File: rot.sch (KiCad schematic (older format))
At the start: 34 parts, among them J3 543630489, J4 M20-7830642, U2 W25Q32JVSSIQ_TR, U3 W25Q32JVSSIQ_TR, U4 W25Q32JVSSIQ_TR, U5 W25Q32JVSSIQ_TR

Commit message: RoT - cleanup
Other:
- note added: "RoT module connector"
- note removed: "RoT connector"
- moved on the sheet: J4
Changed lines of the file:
@@
 	1    0    0    -1
 $EndComp
-Text Notes 2425 1350 0    118  ~ 0
+Text Notes 1425 1250 0    118  ~ 24
 BIOS flash
-Text Notes 2525 6300 0    118  ~ 0
+Text Notes 1625 6175 0    118  ~ 24
 BMC flash
-Text Notes 10900 1500 0    118  ~ 0
+Text Notes 11525 4275 0    118  ~ 24
 TPM connector
 Text Notes 1650 6400 0    50   ~ 0
@@
 Wire Wire Line
 	9675 6025 9175 6025
-Text Notes 8325 4350 0    118  ~ 0
-RoT connector
+Text Notes 7375 4200 0    118  ~ 24
+RoT module connector
 Text Notes 8775 6950 0    50   ~ 0
 preliminary\n
@@
 L artix-dc-scm:M20-7830642 J4
 U 1 1 5FD63CCC
-P 11725 2200
-F 0 "J4" H 11725 2647 60  0000 C CNN
-F 1 "M20-7830642" H 11725 2541 60  0000 C CNN
-F 2 "artix-dc-scm-footprints:PinHeader_6x2_P2.54mm_Vertical" H 11925 2400 60  0001 L CNN
-F 3 "" H 11925 2500 60  0001 L CNN
-F 4 "M20-7830642" H 11925 2700 60  0001 L CNN "MPN"
-F 5 "Molex" H 11925 2800 60  0001 L CNN "Manufacturer"
-	1    11725 2200
-	1    0    0    -1
-$EndComp
-Text GLabel 10900 1950 1    50   Input ~ 0
+P 12475 5250
+F 0 "J4" H 12475 5697 60  0000 C CNN
+F 1 "M20-7830642" H 12475 5591 60  0000 C CNN
+F 2 "artix-dc-scm-footprints:PinHeader_6x2_P2.54mm_Vertical" H 12675 5450 60  0001 L CNN
+F 3 "" H 12675 5550 60  0001 L CNN
+F 4 "M20-7830642" H 12675 5750 60  0001 L CNN "MPN"
+F 5 "Molex" H 12675 5850 60  0001 L CNN "Manufacturer"
+	1    12475 5250
+	1    0    0    -1
+$EndComp
+Text GLabel 11650 5000 1    50   Input ~ 0
 VCC3V3
-Text GLabel 11525 2000 0    50   Input ~ 0
+Text GLabel 12275 5050 0    50   Input ~ 0
 SPI0_CS_N
-Text GLabel 11525 2100 0    50   Input ~ 0
+Text GLabel 12275 5150 0    50   Input ~ 0
 SPI0_MOSI
-Text GLabel 11525 2200 0    50   Input ~ 0
+Text GLabel 12275 5250 0    50   Input ~ 0
 SPI0_MISO
-Text GLabel 11525 2300 0    50   Input ~ 0
+Text GLabel 12275 5350 0    50   Input ~ 0
 SPI0_CLK
-Text GLabel 11925 2000 2    50   Input ~ 0
+Text GLabel 12675 5050 2    50   Input ~ 0
 PIRQ#
-Text GLabel 11925 2100 2    50   Input ~ 0
+Text GLabel 12675 5150 2    50   Input ~ 0
 RST
-Text GLabel 11925 2200 2    50   Input ~ 0
+Text GLabel 12675 5250 2    50   Input ~ 0
 GPIO
-Text GLabel 11925 2300 2    50   Input ~ 0
+Text GLabel 12675 5350 2    50   Input ~ 0
 PP
-Text GLabel 12375 1950 1    50   Input ~ 0
+Text GLabel 13125 5000 1    50   Input ~ 0
 VCC3V3
 Wire Wire Line
-	11525 2500 10900 2500
-Wire Wire Line
-	10900 2500 10900 1950
-Wire Wire Line
-	11925 2500 12375 2500
-Wire Wire Line
-	12375 2500 12375 1950
-Wire Wire Line
-	11525 2400 11400 2400
-Wire Wire Line
-	11400 2400 11400 2650
-Wire Wire Line
-	11925 2400 12050 2400
-Wire Wire Line
-	12050 2400 12050 2650
+	12275 5550 11650 5550
+Wire Wire Line
+	11650 5550 11650 5000
+Wire Wire Line
+	12675 5550 13125 5550
+Wire Wire Line
+	13125 5550 13125 5000
+Wire Wire Line
+	12275 5450 12150 5450
+Wire Wire Line
+	12150 5450 12150 5700
+Wire Wire Line
+	12675 5450 12800 5450
+Wire Wire Line
+	12800 5450 12800 5700
 $Comp
 L artix-dc-scm:GND-artix-dc-scm #PWR?
 U 1 1 5FD8331F
-P 12050 2650
+P 12800 5700
 AR Path="/5FC6B687/5FD8331F" Ref="#PWR?"  Part="1"
 AR Path="/624C566F/5FD8331F" Ref="#PWR025"  Part="1"
-F 0 "#PWR025" H 12050 2400 50  0001 C CNN
-F 1 "GND" H 12055 2477 50  0000 C CNN
-F 2 "" H 12050 2650 50  0001 C CNN
-F 3 "" H 12050 2650 50  0001 C CNN
-	1    12050 2650
-	1    0    0    -1
-$EndComp
-Text Notes 12175 2675 0    50   ~ 0
+F 0 "#PWR025" H 12800 5450 50  0001 C CNN
+F 1 "GND" H 12805 5527 50  0000 C CNN
+F 2 "" H 12800 5700 50  0001 C CNN
+F 3 "" H 12800 5700 50  0001 C CNN
+	1    12800 5700
+	1    0    0    -1
+$EndComp
+Text Notes 12925 5725 0    50   ~ 0
 Pinout for AES-PMOD-TPM20-SLB9670-G
-Text Notes 12325 2425 1    50   ~ 0
+Text Notes 13075 5475 1    50   ~ 0
 TODO: tie this pins to DC-SCI connector
 Wire Wire Line
@@
 L artix-dc-scm:GND-artix-dc-scm #PWR?
 U 1 1 5FD82134
-P 11400 2650
+P 12150 5700
 AR Path="/5FC6B687/5FD82134" Ref="#PWR?"  Part="1"
 AR Path="/624C566F/5FD82134" Ref="#PWR024"  Part="1"
-F 0 "#PWR024" H 11400 2400 50  0001 C CNN
-F 1 "GND" H 11405 2477 50  0000 C CNN
-F 2 "" H 11400 2650 50  0001 C CNN
-F 3 "" H 11400 2650 50  0001 C CNN
-	1    11400 2650
-	1    0    0    -1
-$EndComp
+F 0 "#PWR024" H 12150 5450 50  0001 C CNN
+F 1 "GND" H 12155 5527 50  0000 C CNN
+F 2 "" H 12150 5700 50  0001 C CNN
+F 3 "" H 12150 5700 50  0001 C CNN
+	1    12150 5700
+	1    0    0    -1
+$EndComp

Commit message: Replaced RoT connector with higher one
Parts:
- removed J3: 543630489, artix-dc-scm-footprints:543630489, symbol artix-dc-scm:543630489
- added J3: 529910408, artix-dc-scm-footprints:529910408, symbol artix-dc-scm:529910408
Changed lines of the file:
@@
 Wire Wire Line
 	9175 6525 9775 6525
-$Comp
-L artix-dc-scm:543630489 J3
-U 1 1 6268C044
-P 8925 6775
-F 0 "J3" H 8950 6790 50  0000 C CNN
-F 1 "543630489" H 8950 6699 50  0000 C CNN
-F 2 "artix-dc-scm-footprints:543630489" H 8675 4425 50  0001 C CNN
-F 3 "https://www.molex.com/pdm_docs/sd/543630489_sd.pdf" H 9175 4475 50  0001 C CNN
-	1    8925 6775
-	1    0    0    1
-$EndComp
 Text GLabel 8225 5325 0    50   Input ~ 0
 ROT_QSPI_SCK
@@
 Text GLabel 9675 4625 2    50   Input ~ 0
 ROT_QSPI_CS_B
+$Comp
+L artix-dc-scm:529910408 J3
+U 1 1 61745B1A
+P 8925 6775
+F 0 "J3" H 8950 4360 50  0000 C CNN
+F 1 "529910408" H 8950 4451 50  0000 C CNN
+F 2 "artix-dc-scm-footprints:529910408" H 8675 4425 50  0001 C CNN
+F 3 "https://www.molex.com/pdm_docs/sd/543630489_sd.pdf" H 9175 4475 50  0001 C CNN
+	1    8925 6775
+	1    0    0    1
+$EndComp
 $EndSCHEMATC

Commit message: Add RoT stood
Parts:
- added MP1: PCB_Spacer_M2, antmicro-footprints:9774030243R, symbol antmicroMechanicalParts:PCB_Spacer_M2
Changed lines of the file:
@@
 	1    0    0    1
 $EndComp
+$Comp
+L antmicroMechanicalParts:PCB_Spacer_M2 MP1
+U 1 1 61611FCB
+P 12125 7400
+F 0 "MP1" H 12333 7537 50  0000 L CNN
+F 1 "PCB_Spacer_M2" H 12333 7446 50  0000 L CNN
+F 2 "antmicro-footprints:9774030243R" H 12925 8100 50  0001 C CNN
+F 3 "https://katalog.we-online.de/em/datasheet/9774030243R.pdf" H 13075 8200 50  0001 C CNN
+F 4 "9774030243R" H 12333 7355 50  0000 L CNN "MPN"
+F 5 "Wurth Elektronik " H 12333 7264 50  0000 L CNN "Manufacturer"
+	1    12125 7400
+	1    0    0    -1
+$EndComp
 $EndSCHEMATC

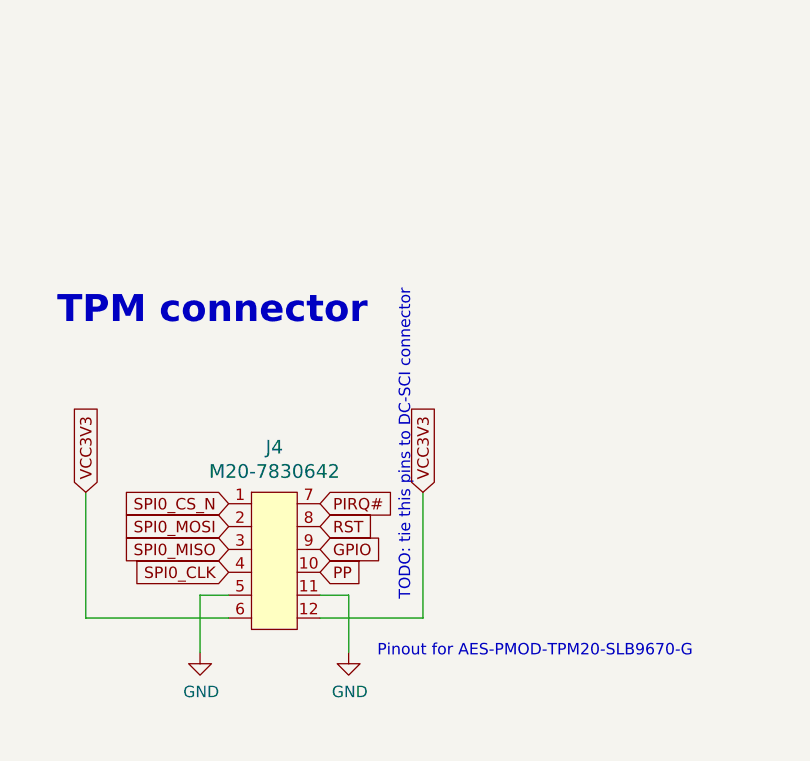
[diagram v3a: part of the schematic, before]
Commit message: Update schematic notes, update SPI0 connection
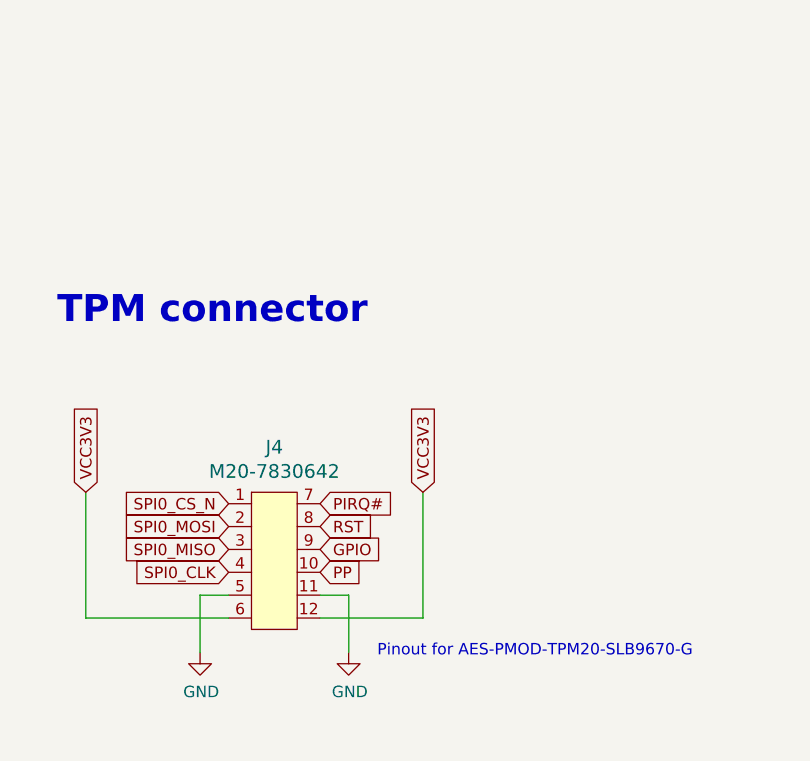
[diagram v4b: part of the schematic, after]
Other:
- note removed: "TODO: tie this pins to DC-SCI connector"
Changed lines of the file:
@@
 Text Notes 12925 5725 0    50   ~ 0
 Pinout for AES-PMOD-TPM20-SLB9670-G
-Text Notes 13075 5475 1    50   ~ 0
-TODO: tie this pins to DC-SCI connector
 Wire Wire Line
 	9675 4825 9175 4825

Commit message: Generated local libs
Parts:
- MP1: footprint antmicro-footprints:9774030243R -> artix-dc-scm-footprints:9774030243R; symbol antmicroMechanicalParts:PCB_Spacer_M2 -> artix-dc-scm:PCB_Spacer_M2
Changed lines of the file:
@@
 $EndComp
 $Comp
-L antmicroMechanicalParts:PCB_Spacer_M2 MP1
+L artix-dc-scm:PCB_Spacer_M2 MP1
 U 1 1 61611FCB
 P 12125 7400
 F 0 "MP1" H 12333 7537 50  0000 L CNN
 F 1 "PCB_Spacer_M2" H 12333 7446 50  0000 L CNN
-F 2 "antmicro-footprints:9774030243R" H 12925 8100 50  0001 C CNN
+F 2 "artix-dc-scm-footprints:9774030243R" H 12925 8100 50  0001 C CNN
 F 3 "https://katalog.we-online.de/em/datasheet/9774030243R.pdf" H 13075 8200 50  0001 C CNN
 F 4 "9774030243R" H 12333 7355 50  0000 L CNN "MPN"

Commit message: Bumped revision to 1.0.1 - replaced ROT connector, added ROT signals and connected to FPGA
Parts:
- removed J3: 529910408, artix-dc-scm-footprints:529910408, symbol artix-dc-scm:529910408
- removed MP1: PCB_Spacer_M2, artix-dc-scm-footprints:9774030243R, symbol artix-dc-scm:PCB_Spacer_M2
- added J8: 52991-0508, antmicro-footprints:529910508, symbol antmicroB2bConnectors:52991-0508
- added SP2: 9774040151, antmicro-footprints:9774040151, symbol antmicroMechanicalParts:9774040151
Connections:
- net labels added: ROT_GPIO1, ROT_GPIO2, ROT_MISO, ROT_MOSI, ROT_RX, ROT_SCLK, ROT_SS, ROT_TX
- wire segments 176 -> 186
- no-connect marks 0 -> 1
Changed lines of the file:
@@
 Title "Artix - Datacenter Secure Control Module (DC-SCM)"
 Date ""
-Rev "1.0.0"
+Rev "1.0.1"
 Comp ""
 Comment1 ""
@@
 	8725 5025 8225 5025
 Wire Wire Line
-	9175 5825 9675 5825
-Wire Wire Line
-	9175 5725 9675 5725
-Wire Wire Line
-	9175 5625 9675 5625
-Wire Wire Line
-	9175 5525 9675 5525
-Wire Wire Line
-	9175 5325 9675 5325
-Wire Wire Line
-	9175 5225 9675 5225
-Wire Wire Line
-	9175 5125 9675 5125
-Wire Wire Line
-	9175 5025 9675 5025
-Wire Wire Line
 	8725 4925 8225 4925
 Wire Wire Line
-	9175 5925 9675 5925
-Wire Wire Line
-	9175 5425 9675 5425
-Wire Wire Line
-	9175 4925 9675 4925
-Wire Wire Line
 	8725 5525 8225 5525
-Wire Wire Line
-	9675 6325 9175 6325
-Wire Wire Line
-	9675 6225 9175 6225
-Wire Wire Line
-	9675 6125 9175 6125
-Wire Wire Line
-	9675 6025 9175 6025
-Text Notes 7975 4225 0    118  ~ 24
+Text Notes 8150 3825 0    118  ~ 24
 RoT module connector
-Text Notes 8775 6950 0    50   ~ 0
+Text Notes 9025 7000 0    50   ~ 0
 preliminary\n
 Text GLabel 8225 4625 0    50   Input ~ 0
@@
 Pinout for AES-PMOD-TPM20-SLB9670-G
 Wire Wire Line
-	9675 4825 9175 4825
-Wire Wire Line
-	9675 4725 9175 4725
-Wire Wire Line
-	9675 4625 9175 4625
-Wire Wire Line
 	8725 4825 8225 4825
 Wire Wire Line
@@
 Text GLabel 8225 4725 0    50   Input ~ 0
 INIT
-Text GLabel 9775 6525 2    50   Input ~ 0
-VCC3V3
-Wire Wire Line
-	8225 6525 8725 6525
+Text GLabel 9775 6625 2    50   Input ~ 0
+VCC3V3
 $Comp
 L artix-dc-scm:GND-artix-dc-scm #PWR?
 U 1 1 626717FC
-P 8225 6525
+P 8725 7075
 AR Path="/5FC6B687/626717FC" Ref="#PWR?"  Part="1"
 AR Path="/624C566F/626717FC" Ref="#PWR0110"  Part="1"
-F 0 "#PWR0110" H 8225 6275 50  0001 C CNN
-F 1 "GND" H 8230 6352 50  0000 C CNN
-F 2 "" H 8225 6525 50  0001 C CNN
-F 3 "" H 8225 6525 50  0001 C CNN
-	1    8225 6525
-	0    1    -1   0
-$EndComp
-Wire Wire Line
-	9175 6525 9775 6525
+F 0 "#PWR0110" H 8725 6825 50  0001 C CNN
+F 1 "GND" H 8730 6902 50  0000 C CNN
+F 2 "" H 8725 7075 50  0001 C CNN
+F 3 "" H 8725 7075 50  0001 C CNN
+	1    8725 7075
+	-1   0    0    -1
+$EndComp
 Text GLabel 8225 5325 0    50   Input ~ 0
 ROT_QSPI_SCK
@@
 Wire Wire Line
 	8725 5325 8225 5325
-Wire Wire Line
-	9175 6425 9675 6425
 Text GLabel 9675 6425 2    50   Input ~ 0
 QSPI0_CS1_N
@@
 Text GLabel 9675 4625 2    50   Input ~ 0
 ROT_QSPI_CS_B
-$Comp
-L artix-dc-scm:529910408 J3
-U 1 1 61745B1A
-P 8925 6775
-F 0 "J3" H 8950 4360 50  0000 C CNN
-F 1 "529910408" H 8950 4451 50  0000 C CNN
-F 2 "artix-dc-scm-footprints:529910408" H 8675 4425 50  0001 C CNN
-F 3 "https://www.molex.com/pdm_docs/sd/543630489_sd.pdf" H 9175 4475 50  0001 C CNN
-	1    8925 6775
+Wire Wire Line
+	9675 6025 9175 6025
+Wire Wire Line
+	9675 6125 9175 6125
+Wire Wire Line
+	9675 6225 9175 6225
+Wire Wire Line
+	9675 6325 9175 6325
+Wire Wire Line
+	9175 6425 9675 6425
+Wire Wire Line
+	9175 6625 9775 6625
+Wire Wire Line
+	9675 4625 9175 4625
+Wire Wire Line
+	9675 4725 9175 4725
+Wire Wire Line
+	9675 4825 9175 4825
+Wire Wire Line
+	9175 4925 9675 4925
+Wire Wire Line
+	9175 5025 9675 5025
+Wire Wire Line
+	9175 5125 9675 5125
+Wire Wire Line
+	9175 5225 9675 5225
+Wire Wire Line
+	9175 5325 9675 5325
+Wire Wire Line
+	9175 5425 9675 5425
+Wire Wire Line
+	9175 5525 9675 5525
+Wire Wire Line
+	9175 5625 9675 5625
+Wire Wire Line
+	9175 5725 9675 5725
+Wire Wire Line
+	9175 5825 9675 5825
+Wire Wire Line
+	9175 5925 9675 5925
+$Comp
+L antmicroB2bConnectors:52991-0508 J8
+U 1 1 6010D4E5
+P 8925 6975
+F 0 "J8" H 8950 4060 50  0000 C CNN
+F 1 "52991-0508" H 8950 4151 50  0000 C CNN
+F 2 "antmicro-footprints:529910508" H 10475 5275 50  0001 C CNN
+F 3 "https://www.molex.com/pdm_docs/sd/529910508_sd.pdf" H 9175 5175 50  0001 C CNN
+	1    8925 6975
 	1    0    0    1
 $EndComp
-$Comp
-L artix-dc-scm:PCB_Spacer_M2 MP1
-U 1 1 61611FCB
-P 12125 7400
-F 0 "MP1" H 12333 7537 50  0000 L CNN
-F 1 "PCB_Spacer_M2" H 12333 7446 50  0000 L CNN
-F 2 "artix-dc-scm-footprints:9774030243R" H 12925 8100 50  0001 C CNN
-F 3 "https://katalog.we-online.de/em/datasheet/9774030243R.pdf" H 13075 8200 50  0001 C CNN
-F 4 "9774030243R" H 12333 7355 50  0000 L CNN "MPN"
-F 5 "Wurth Elektronik " H 12333 7264 50  0000 L CNN "Manufacturer"
-	1    12125 7400
-	1    0    0    -1
-$EndComp
+Text GLabel 8225 6525 0    50   Input ~ 0
+ROT_GPIO2
+Wire Wire Line
+	8725 6525 8225 6525
+Text GLabel 8225 4525 0    50   Input ~ 0
+ROT_TX
+Wire Wire Line
+	8725 4525 8225 4525
+Text GLabel 8225 4425 0    50   Input ~ 0
+ROT_RX
+Wire Wire Line
+	8725 4425 8225 4425
+Text GLabel 8225 4325 0    50   Input ~ 0
+ROT_SCLK
+Wire Wire Line
+	8725 4325 8225 4325
+Text GLabel 9675 4325 2    50   Input ~ 0
+ROT_MOSI
+Wire Wire Line
+	9175 4325 9675 4325
+Text GLabel 9675 4425 2    50   Input ~ 0
+ROT_MISO
+Wire Wire Line
+	9175 4425 9675 4425
+Text GLabel 9675 4525 2    50   Input ~ 0
+ROT_SS
+Wire Wire Line
+	9175 4525 9675 4525
+Wire Wire Line
+	8725 6625 8725 6725
+Wire Wire Line
+	8725 6725 8725 7075
+Connection ~ 8725 6725
+Wire Wire Line
+	9175 6725 9175 6625
+Connection ~ 9175 6625
+Wire Wire Line
+	9175 6525 9675 6525
+Text GLabel 9675 6525 2    50   Input ~ 0
+ROT_GPIO1
+$Comp
+L antmicroMechanicalParts:9774040151 SP2
+U 1 1 602968FE
+P 9875 7050
+F 0 "SP2" H 10005 7103 60  0000 L CNN
+F 1 "9774040151" H 10005 6997 60  0000 L CNN
+F 2 "antmicro-footprints:9774040151" H 9875 7050 60  0001 C CNN
+F 3 "https://www.we-online.com/catalog/datasheet/9774040151.pdf" H 9875 7050 60  0001 C CNN
+F 4 "Wurth Elektronik" H 9875 7050 50  0001 C CNN "Manufacturer"
+F 5 "9774030151" H 9875 7050 50  0001 C CNN "MPN"
+	1    9875 7050
+	1    0    0    -1
+$EndComp
+NoConn ~ 9675 7050
 $EndSCHEMATC

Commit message: Update edge connector
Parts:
- J8: footprint antmicro-footprints:529910508 -> artix-dc-scm-footprints:529910508; symbol antmicroB2bConnectors:52991-0508 -> artix-dc-scm:52991-0508
- SP2: footprint antmicro-footprints:9774040151 -> artix-dc-scm-footprints:9774040151; symbol antmicroMechanicalParts:9774040151 -> artix-dc-scm:9774040151
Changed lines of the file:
@@
 	9175 5925 9675 5925
 $Comp
-L antmicroB2bConnectors:52991-0508 J8
+L artix-dc-scm:52991-0508 J8
 U 1 1 6010D4E5
 P 8925 6975
 F 0 "J8" H 8950 4060 50  0000 C CNN
 F 1 "52991-0508" H 8950 4151 50  0000 C CNN
-F 2 "antmicro-footprints:529910508" H 10475 5275 50  0001 C CNN
+F 2 "artix-dc-scm-footprints:529910508" H 10475 5275 50  0001 C CNN
 F 3 "https://www.molex.com/pdm_docs/sd/529910508_sd.pdf" H 9175 5175 50  0001 C CNN
 	1    8925 6975
@@
 ROT_GPIO1
 $Comp
-L antmicroMechanicalParts:9774040151 SP2
+L artix-dc-scm:9774040151 SP2
 U 1 1 602968FE
 P 9875 7050
 F 0 "SP2" H 10005 7103 60  0000 L CNN
 F 1 "9774040151" H 10005 6997 60  0000 L CNN
-F 2 "antmicro-footprints:9774040151" H 9875 7050 60  0001 C CNN
+F 2 "artix-dc-scm-footprints:9774040151" H 9875 7050 60  0001 C CNN
 F 3 "https://www.we-online.com/catalog/datasheet/9774040151.pdf" H 9875 7050 60  0001 C CNN
 F 4 "Wurth Elektronik" H 9875 7050 50  0001 C CNN "Manufacturer"
